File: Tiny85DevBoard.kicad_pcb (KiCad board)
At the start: 2 copper layers, 25.9 x 37.8 mm, 13 parts, among them J1 Screw_Terminal_01x02, J2 AVR-ISP-6, J3 Conn_01x04_Female, J4 Conn_01x04_Female, SW1 SW_SPDT, SW2 Reset, U1 LD1117S33TR_SOT223, U2 ATtiny85-20PU

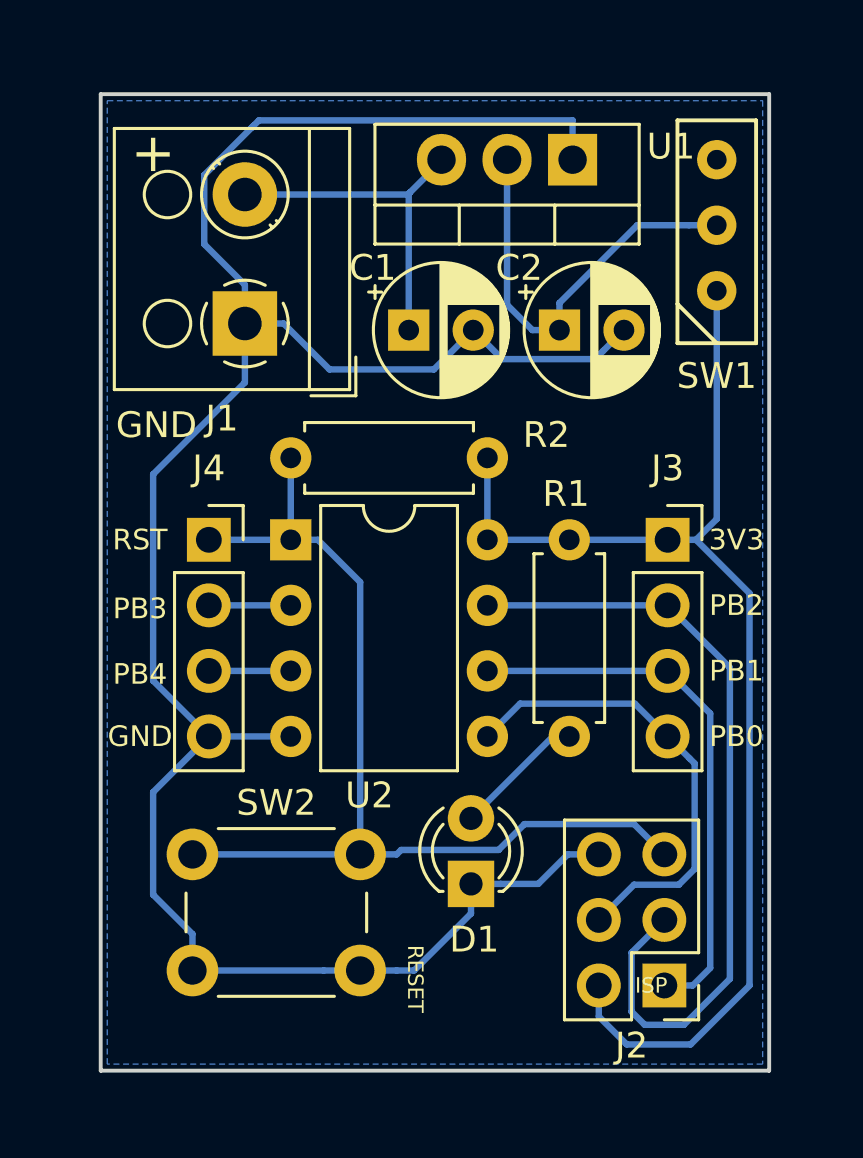
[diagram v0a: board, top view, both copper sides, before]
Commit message: Adjusted size of component holes.
The component holes used default sizes from the footprints, which
were mostly too large for my components. Adjusted hole dimensions.
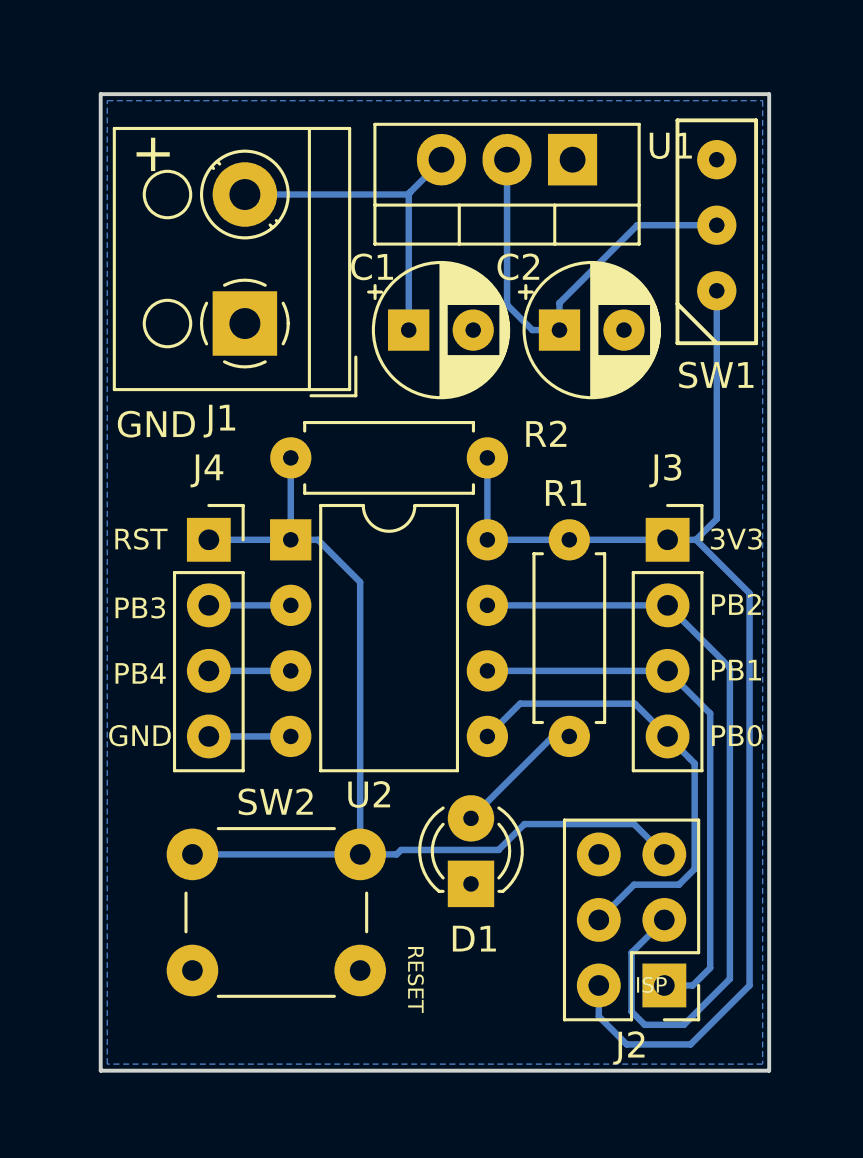
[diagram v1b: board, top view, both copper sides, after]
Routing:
- net GNDPWR: track 91.3 -> 3.86 mm

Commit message: Made board outline bigger.
Some of the traces were too close to the edge of the board.
Enlarged the edge cuts to give a bigger margin for safety.
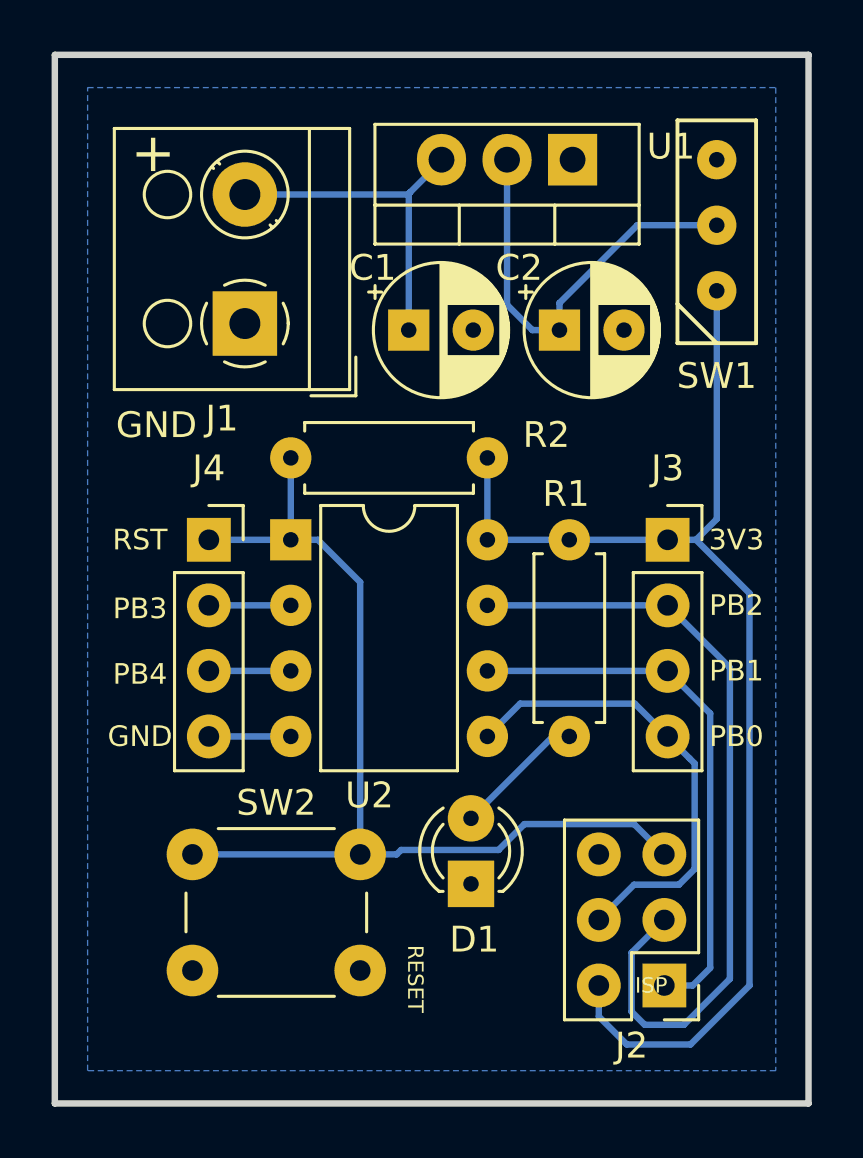
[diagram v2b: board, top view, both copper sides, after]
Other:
- board size 25.9 x 37.8 mm -> 29.2 x 40.6 mm
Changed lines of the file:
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@@
   (general
     (thickness 1.6)
-    (drawings 22)
+    (drawings 16)
     (tracks 64)
     (zones 0)
@@
     (visible_elements FFFFFF7F)
     (pcbplotparams
-      (layerselection 0x01020_fffffffe)
+      (layerselection 0x01120_fffffffe)
       (usegerberextensions false)
       (usegerberattributes false)
@@
       (subtractmaskfromsilk false)
       (outputformat 5)
-      (mirror true)
+      (mirror false)
       (drillshape 2)
       (scaleselection 1)
@@
     )
   )
-  (gr_line (start 162.56 89.916) (end 165.1 89.916) (layer Dwgs.User) (width 0.2))
-  (gr_line (start 162.56 92.456) (end 162.56 89.916) (layer Dwgs.User) (width 0.2))
-  (gr_line (start 189.484 129.032) (end 186.944 129.032) (layer Dwgs.User) (width 0.2))
-  (gr_line (start 189.484 126.492) (end 189.484 129.032) (layer Dwgs.User) (width 0.2))
-  (target plus (at 159.512 125.984) (size 5) (width 0.15) (layer Edge.Cuts))
-  (target plus (at 192.024 92.964) (size 5) (width 0.15) (layer Edge.Cuts))
   (gr_text ISP (at 184.404 124.968) (layer F.SilkS)
     (effects (font (size 0.6 0.6) (thickness 0.15)))
@@
     (effects (font (size 1.5 1.5) (thickness 0.3)))
   )
-  (gr_line (start 163.068 128.27) (end 163.068 90.424) (layer Edge.Cuts) (width 0.15))
-  (gr_line (start 188.976 128.27) (end 163.068 128.27) (layer Edge.Cuts) (width 0.15))
-  (gr_line (start 188.976 90.424) (end 188.976 128.27) (layer Edge.Cuts) (width 0.15))
-  (gr_line (start 163.068 90.424) (end 188.976 90.424) (layer Edge.Cuts) (width 0.15))
+  (gr_line (start 161.29 129.54) (end 161.29 88.9) (layer Edge.Cuts) (width 0.25))
+  (gr_line (start 190.5 129.54) (end 161.29 129.54) (layer Edge.Cuts) (width 0.25))
+  (gr_line (start 190.5 88.9) (end 190.5 129.54) (layer Edge.Cuts) (width 0.25))
+  (gr_line (start 161.29 88.9) (end 190.5 88.9) (layer Edge.Cuts) (width 0.25))
   (segment (start 178.054 104.521) (end 178.054 107.696) (width 0.25) (layer B.Cu) (net 1) (status 30))
   (segment (start 178.054 107.696) (end 181.229 107.696) (width 0.25) (layer B.Cu) (net 1) (status 30))
@@
     (polygon
       (pts
-        (xy 163.322 90.678) (xy 188.722 90.678) (xy 188.722 128.016) (xy 163.322 128.016)
+        (xy 162.56 90.17) (xy 189.23 90.17) (xy 189.23 128.27) (xy 162.56 128.27)
       )
     )
